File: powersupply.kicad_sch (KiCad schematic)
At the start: 3 parts, among them J1 Screw_Terminal_01x02, U1 3V3, U2 5V

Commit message: add gitignore
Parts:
- renumbered J1 to J10

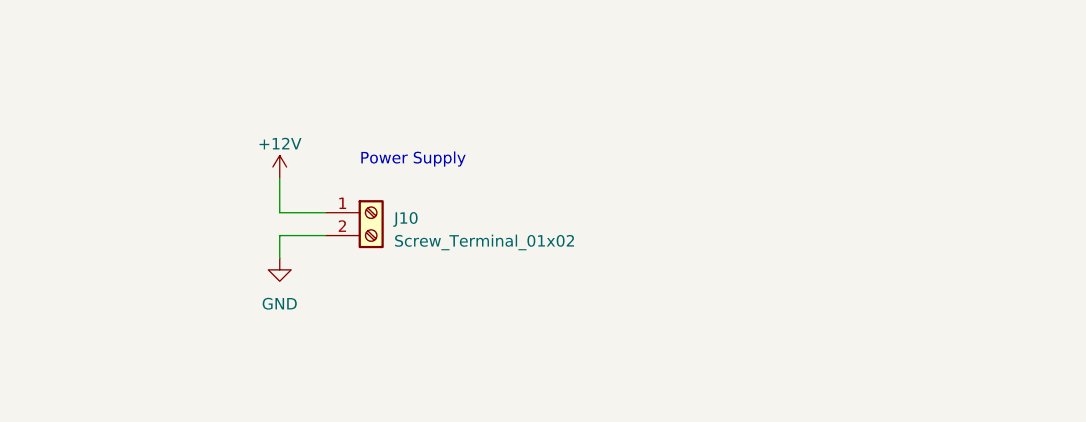
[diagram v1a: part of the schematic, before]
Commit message: Add input protection, fix USB-C/CP2102 supply, harden optocoupler input
Power supply:
- Add 12V input protection: PTC fuse F1 (1.1A/33V, C70119), TVS D6
  (SMAJ15CA, C151939), reverse polarity Schottky D7 (SS34, C8678) and
  bulk cap C13 (100uF/25V, C179802)

USB2RS232:
- Power CP2102N (VDD/REGIN) from +3.3V via R25 (0R)
- Add 5k1 pull-downs R23/R24 on USB-C CC1/CC2 so C-to-C hosts supply VBUS

ESP32 / Interfaces:
- Add 100k gate pull-downs R26/R27/R28 on Q2/Q1/Q3 (relay, LED, buzzer
  stay off during reset/boot)
- Buzzer flyback D1: 1N4148W SOD-123 (C81598) instead of undefined SOT-23
- WAKE_UP input (J8/U3): series zener D8 (BZT52C6V8, C173404), reverse
  polarity diode D9 (1N4148W), R11 = 1k5 0805 (C4310); switches at ~9V,
  safe up to 14.4V
- IC1 value set to ESP32-S3-WROOM-1U to match footprint
- Add no-connect flags on unused ESP32, J99 and K1 pins
- Remove duplicate local labels IO_PUMP_LED/IO_PUMP_RELAIS
- Move off-grid symbols, labels and wires onto grid

PCB: update from schematic
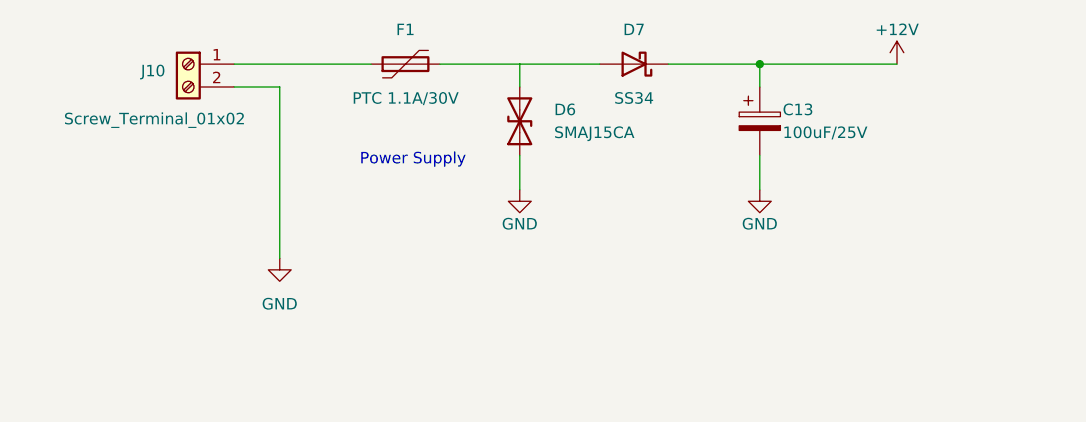
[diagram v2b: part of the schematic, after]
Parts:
- added C13: 100uF/25V, Capacitor_SMD:CP_Elec_6.3x7.7, symbol Device:C_Polarized
- added D6: SMAJ15CA, Diode_SMD:D_SMA, symbol Device:D_TVS
- added D7: SS34, Diode_SMD:D_SMA, symbol Device:D_Schottky
- added F1: PTC 1.1A/30V, Fuse:Fuse_1812_4532Metric, symbol Device:Polyfuse
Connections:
- net +12V: now also C13.1, D7.1 (K); no longer J10.1 (Pin_1)
- net GND: now also C13.2, D6.1 (A1)
- new net: F1.1, J10.1 (Pin_1)
- new net: D6.2 (A2), D7.2 (A), F1.2
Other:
- moved on the sheet: J10

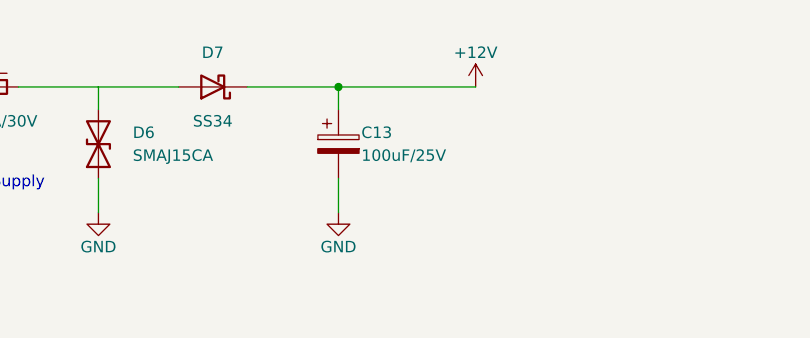
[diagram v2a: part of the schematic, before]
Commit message: Add native ESP32-S3 USB port, move buzzer driver to Interfaces sheet
ESP32:
- Add USB-C J4 for ESP32-S3 native USB (USB-Serial-JTAG):
  D+ -> GPIO20, D- -> GPIO19 via 0R series resistors R31/R32 (0402, C17168),
  ESD diodes D10/D12 (LESD5D5.0CT1G), CC pull-downs R29/R30 5k1,
  VBUS not connected (no-connect flag)
- Move JTAG header J99 and decoupling C10-C12 to free space for J4

Interfaces:
- Move buzzer driver (Q3, R6, R28, R2, R7, D1, BZ1) from ESP32 sheet
- Make IO_BUZZER a global label so GPIO4 still reaches R6/Q3
- Shift optocoupler input block (J8, D8, D9, R11, R12, U3) down

Power supply:
- Add PWR_FLAG on +12V after reverse polarity diode D7 (ERC clean)

PCB: update from schematic
ERC: 0 errors, 5 warnings (2N7002 symbol lib mismatch, unused RFID_IRQ/RST)
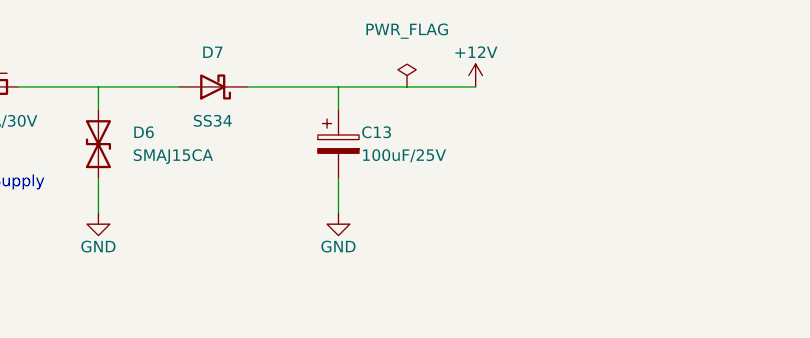
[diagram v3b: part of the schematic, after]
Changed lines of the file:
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@@
 		)
-	)
-	(junction
-		(at 92.71 30.48)
-		(diameter 0)
-		(color 0 0 0 0)
 	)
 	(wire
@@
 		(pts
 			(xy 199.39 102.87) (xy 210.82 102.87)
-		)
-		(stroke
-			(width 0)
-			(type default)
-		)
-	)
-	(wire
-		(pts
-			(xy 92.71 30.48) (xy 107.95 30.48)
 		)
 		(stroke
@@
 		)
 	)
+	(symbol
+		(lib_id "power:PWR_FLAG")
+		(at 100.33 30.48 0)
+		(unit 1)
+		(body_style 1)
+		(exclude_from_sim no)
+		(in_bom yes)
+		(on_board yes)
+		(in_pos_files yes)
+		(dnp no)
+		(property "Reference" "#FLG01"
+			(at 100.33 32.385 0)
+			(hide yes)
+			(show_name no)
+			(do_not_autoplace no)
+			(effects
+				(font
+					(size 1.27 1.27)
+				)
+			)
+		)
+		(property "Value" "PWR_FLAG"
+			(at 100.33 24.13 0)
+			(show_name no)
+			(do_not_autoplace no)
+			(effects
+				(font
+					(size 1.27 1.27)
+				)
+			)
+		)
+		(property "Footprint" ""
+			(at 100.33 30.48 0)
+			(hide yes)
+			(show_name no)
+			(do_not_autoplace no)
+			(effects
+				(font
+					(size 1.27 1.27)
+				)
+			)
+		)
+		(property "Datasheet" ""
+			(at 100.33 30.48 0)
+			(hide yes)
+			(show_name no)
+			(do_not_autoplace no)
+			(effects
+				(font
+					(size 1.27 1.27)
+				)
+			)
+		)
+		(property "Description" "Special symbol for telling ERC where power comes from"
+			(at 100.33 30.48 0)
+			(hide yes)
+			(show_name no)
+			(do_not_autoplace no)
+			(effects
+				(font
+					(size 1.27 1.27)
+				)
+			)
+		)
+		(pin "1"
+		)
+		(instances
+			(project "GA_Fuelstation_Terminal"
+				(path "/9d5c9b65-fa9a-4f2b-b8e4-a4447f224f28/93d867b5-46d3-4401-8a12-5d31278231a8"
+					(reference "#FLG01")
+					(unit 1)
+				)
+			)
+		)
+	)
+	(wire
+		(pts
+			(xy 92.71 30.48) (xy 100.33 30.48)
+		)
+		(stroke
+			(width 0)
+			(type default)
+		)
+	)
+	(wire
+		(pts
+			(xy 100.33 30.48) (xy 107.95 30.48)
+		)
+		(stroke
+			(width 0)
+			(type default)
+		)
+	)
